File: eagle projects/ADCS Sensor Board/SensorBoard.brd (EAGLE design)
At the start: 91 x 91 mm, 134 parts, among them J5 HDR_10_EZFET_DEBUGGER, J6 MTI-1_8428-11B1-RK-TP, Q1 BC850SMD, Q2 IRF7507TRPBF, Q3 BSS138PS,115, Q4 BSS138PS,115, Q5 BSS138PS,115, Q6 BSS138PS,115, U1 MSP430F5529IPN, U2 LMV321, U3 ADS7841E_2K5, U4 LMV321, U5 LM20BIM7X_NOPB, U6 LMV321, U7 TLV9054IDR, U8 REF194GSZ-REEL7, U9 ADS7841E_2K5, Y1 32.768kHz, Y2 CSTCR4M00G15L99

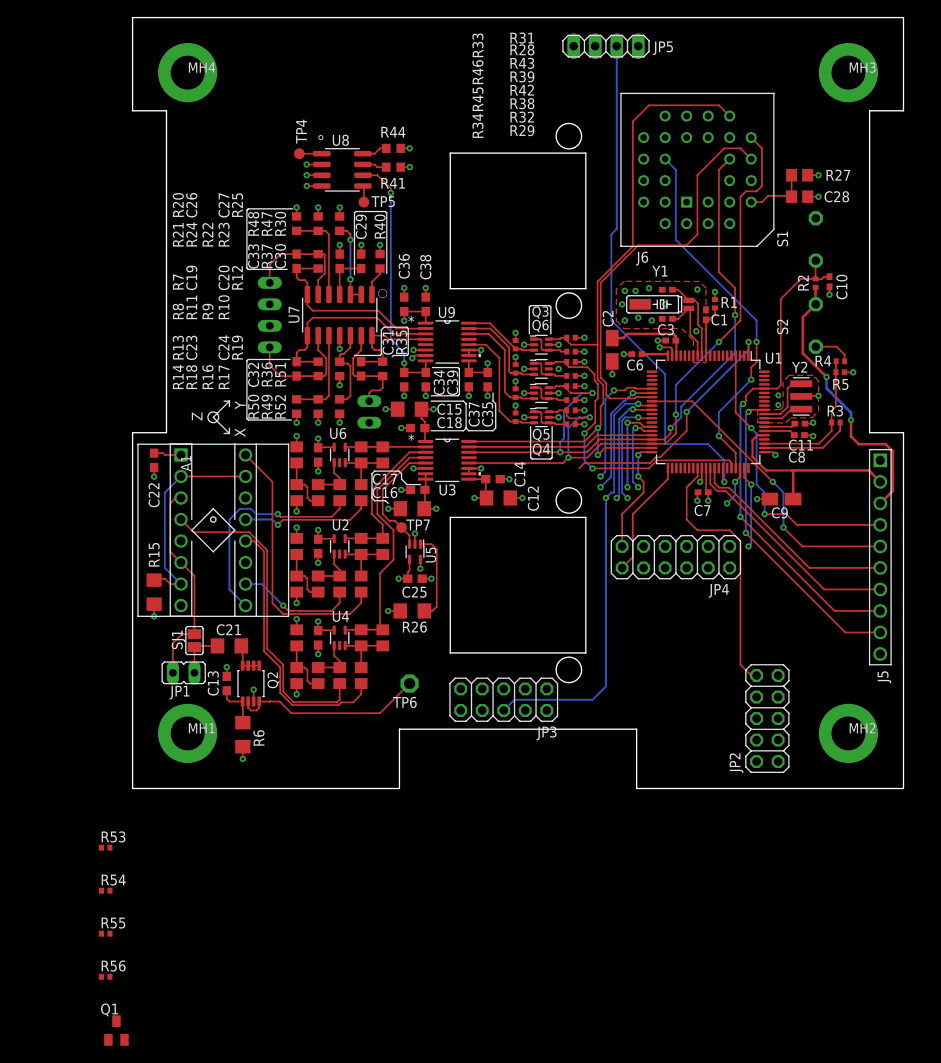
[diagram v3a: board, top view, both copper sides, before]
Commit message: Added files for Sunsensor Boards
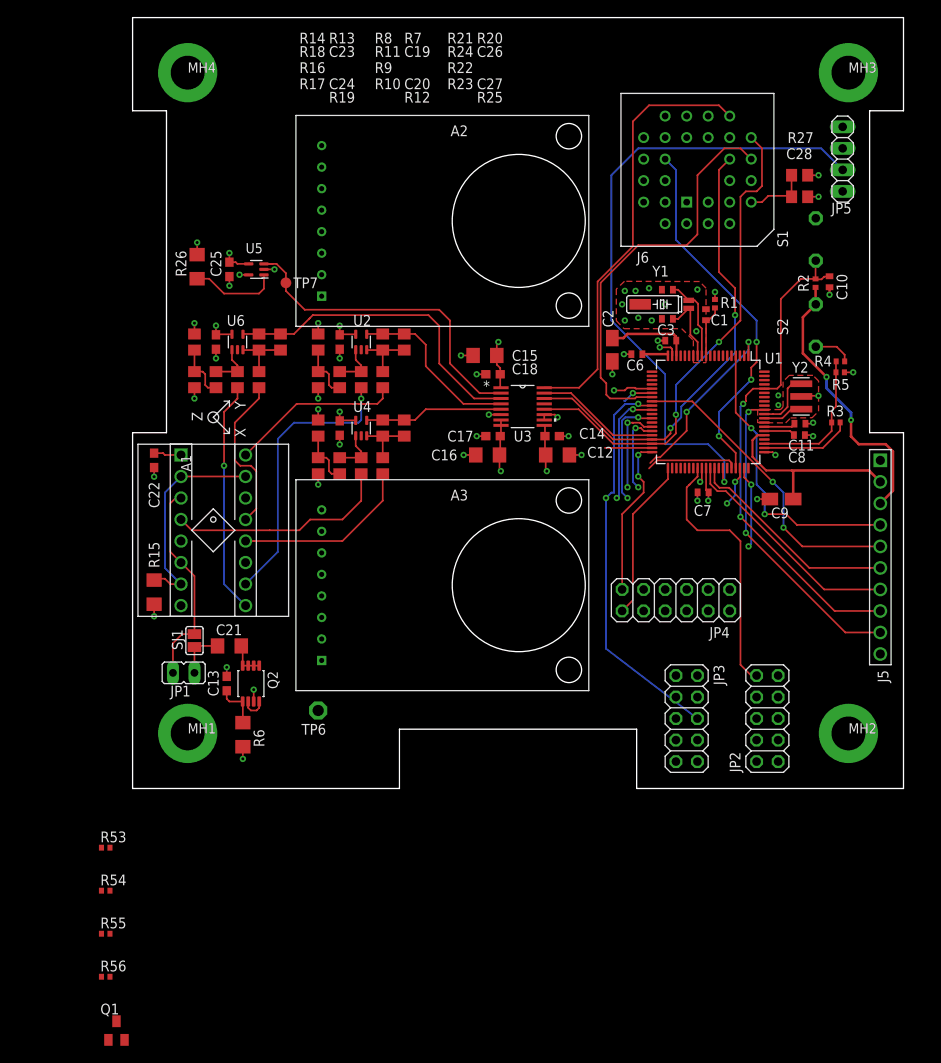
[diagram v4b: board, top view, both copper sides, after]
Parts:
- removed C29: 4.7u, rcl:C0603
- removed C30, C37, C38, C39: 0.1u, rcl:C0603
- removed C31, C32, C33: 9.1p, rcl:C0603
- removed C34, C35, C36: 1u, rcl:C0603
- removed D1, D2, D3: SFH2430, my_library:JP1Y_LED_SCREEN
- removed Q3, Q4, Q5, Q6: BSS138PS,115, my_library:SOT23-6P65_200X110L30X25N_BSS138PS,115
- removed R28, R29, R31, R32, R33, R34, R38, R39, R42, R43, R45, R46: 10k, rcl:R0402
- removed R30, R40, R41, R44: 5.1M, rcl:R0603
- removed R35, R36, R37: 698k, rcl:R0603
- removed R47, R48, R49, R50, R51, R52: 13.7k, rcl:R0603
- removed TP4, TP5: TPB1,27, testpad:B1,27
- removed U7: TLV9054IDR, my_library:SOIC14P127_865X600X175L83X41N_TLV9054IDR
- removed U8: REF194GSZ-REEL7, my_library:SOIC8P127_490X600X175L83X41N_REF194GSZ-REEL7
- removed U9: ADS7841E_2K5, my_library:DBQ16
- added A2, A3: ARDUCAM_OV5642, my_library:ARDUCAM
- C1, C10, C11, C3, C4, C5, C6, C7, C8: device rcl:0402 -> rcl:C0402
- moved R26 47.9 mm to (7.62, 61.6), turned to 270 degrees
- moved C25 42.6 mm to (11.4, 61.3), turned to 90 degrees
- moved U5 38.2 mm to (14.6, 61.3), turned to 90 degrees
- moved TP7 32.0 mm to (18.1, 59.7), turned to 90 degrees
- moved JP5 31.0 mm to (83.8, 74.3), turned to 270 degrees
- moved C23 24.9 mm to (24.4, 42.5)
- moved C24 24.9 mm to (29.5, 42.5)
- moved R13 24.9 mm to (21.9, 42.5)
- moved R14 24.9 mm to (21.9, 38.1)
- moved R16 24.9 mm to (27.0, 38.1)
- moved R17 24.9 mm to (29.5, 38.1)
- moved R18 24.9 mm to (24.4, 38.1)
- moved R19 24.9 mm to (32.1, 42.5)
- moved U4 24.9 mm to (27.0, 42.5)
- moved C19 24.3 mm to (24.4, 52.7)
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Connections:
- removed net +4V5: C34.1, C39.1, U8.6, U9.8
- removed net 0_DEGREES: C33.2, R37.2, U7.7, U9.2
- removed net 120_DEGREES: C32.2, R36.2, U7.8, U9.3
- removed net 240_DEGREES: C31.2, R35.2, U7.14, U9.4
- removed net 5V_!CS!_SUN_Z-: Q6.3, R46.1, U9.15
- removed net 5V_SPI_CLK: Q3.3, R33.1, U9.16
- removed net 5V_SPI_MISO: Q4.3, R34.1, U9.12
- removed net 5V_SPI_MOSI: Q5.3, R45.1, U9.14
- removed net IN2+BIAS: R47.1, R48.2, U7.5
- removed net IN3+BIAS: R49.1, R50.2, U7.10
- removed net IN4+BIAS: R51.1, R52.2, U7.12
- removed net N$14: Q3.1, Q3.4, R28.2
- removed net N$26: R30.2, U7.2, U7.3
- removed net N$27: R40.1, U7.1
- removed net N$28: C31.1, D3.1, R35.1, U7.13
- removed net N$30: Q5.1, Q5.4, R38.2
- removed net N$31: C32.1, D2.1, R36.1, U7.9
- removed net N$32: C33.1, D1.1, R37.1, U7.6
- removed net N$33: TP5.TP, U8.5
- removed net N$34: TP4.TP, U8.1
- removed net N$41: R41.2, U8.7
- removed net N$42: Q6.1, Q6.4, R39.2
- removed net N$43: R44.2, U8.8
- removed net N$48: Q4.1, Q4.4, R29.2
- new net !CS!_CAM_A: A2.1
- new net !CS!_CAM_B: A3.1
- new net N$17: A3.6
- new net PAYLOAD_MISO: A2.3, A3.3
- new net PAYLOAD_MOSI: A2.2, A3.2
- new net PAYLOAD_SCL: A2.8, A3.8
- new net PAYLOAD_SCLK: A2.4, A3.4
- new net PAYLOAD_SDA: A2.7, A3.7
- net !CS!_SUN_Z-: no longer Q6.6, R43.1
- net +3V3: no longer Q3.2, Q3.5, Q4.2, Q4.5, Q5.2, Q5.5, Q6.2, Q6.5, R28.1, R29.1, R31.2, R32.2, R38.1, R39.1, R42.2, R43.2
- net +5V: now also A2.6; no longer C29.1, C30.1, C35.1, C36.1, C37.1, C38.1, R33.2, R34.2, R45.2, R46.2, R47.2, R49.2, R51.2, U7.4, U8.2, U8.3, U9.1, U9.7, U9.9
- net BRD_TEMP_MEAS: now also U3.2; no longer U3.5
- net B_MEAS_X: now also U3.5; no longer U3.4
- net B_MEAS_Y: now also U3.4; no longer U3.3
- net B_MEAS_Z: now also U3.3; no longer U3.2
- net GND: now also A2.5, A3.5; no longer C29.2, C30.2, C34.2, C35.2, C36.2, C37.2, C38.2, C39.2, D1.2, D2.2, D3.2, R30.1, R40.2, R41.1, R44.1, R48.1, R50.1, R52.1, U7.11, U8.4, U9.10, U9.11, U9.6
- net UCB0_SPI_CLK: no longer Q3.6, R31.1
- net UCB0_SPI_MISO: no longer Q4.6, R32.1
- net UCB0_SPI_MOSI: no longer Q5.6, R42.1
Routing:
- net +4V5: track 30.2 -> 0.00 mm, vias 2 -> 0
- net B_MEAS_Z: track 9.46 -> 38.0 mm
- net HMC1053_RESET: track 52.5 -> 24.1 mm
- net +5V: track 50.7 -> 23.4 mm, vias 12 -> 0
- net UCB0_SPI_CLK: track 83.4 -> 56.5 mm, vias 2 -> 0
- net BRD_TEMP_MEAS: track 14.5 -> 40.0 mm
- net !CS!_SUN_Z-: track 36.1 -> 10.9 mm, vias 2 -> 0
- net 120_DEGREES: track 23.0 -> 0.00 mm
- net GND: track 70.3 -> 47.4 mm, vias 67 -> 48
- net UCB0_SPI_MOSI: track 77.0 -> 54.1 mm, vias 4 -> 2
- net 0_DEGREES: track 22.9 -> 0.00 mm
- net UCB0_SPI_MISO: track 78.7 -> 58.1 mm, vias 4 -> 2
- net OUT_A_N: track 14.1 -> 33.3 mm
- net +3V3: track 105.9 -> 90.0 mm, vias 32 -> 16
- net 5V_SPI_MISO: track 15.1 -> 0.00 mm
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- removed copper zone on layer 15, net +5V
- removed copper zone on layer 15, net +GND
- removed copper zone on layer 15, net GND
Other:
- outline, holes or cut-outs redrawn
- board text added: "Dalhousie Space Systems Lab"
- board text removed: "Q3"
- board text removed: "Q4"
- board text removed: "Q5"
- board text removed: "Q6"

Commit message: removed unused usb stuff from msp430
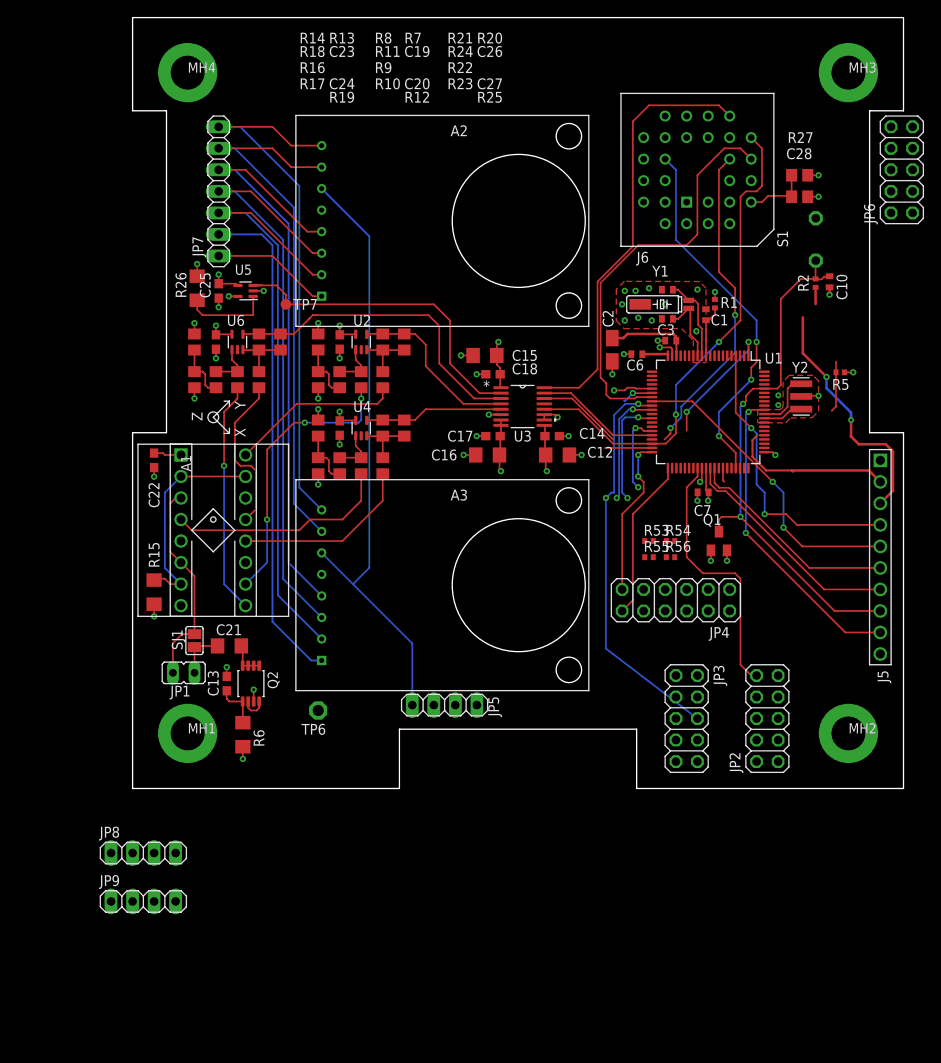
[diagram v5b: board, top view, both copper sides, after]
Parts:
- removed C11, C8: 220n, rcl:C0402
- removed C9: 4u7, rcl:A/3216-18R
- removed R3: 1k4, rcl:R0402
- removed R4: 100R, rcl:R0402
- removed S2: BSL, electricalmeter:PBTH
- added JP6: (no value), pinhead:2X05
- added JP7: (no value), pinhead:1X07
- added JP8, JP9: (no value), pinhead:1X04
- moved Q1 91.6 mm to (69.2, 29.2)
- moved R56 83.1 mm to (63.5, 27.3)
- moved JP5 79.8 mm to (36.8, 9.84), turned to 0 degrees
- moved R54 78.4 mm to (63.5, 29.2)
- moved R55 78.0 mm to (61.0, 27.3)
- moved R53 73.6 mm to (61.0, 29.2)
- moved C25 2.84 mm to (10.2, 58.7)
- moved U5 2.84 mm to (13.3, 58.7)
- moved R26 2.54 mm to (7.62, 59.1)
- moved TP7 2.54 mm to (18.1, 57.1)
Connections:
- removed net N$17: A3.6
- removed net P1.2: U1.23
- removed net P1.3: U1.24
- removed net P4.2: U1.47
- removed net P6.0: U1.77
- removed net P6.1: U1.78
- removed net P6.2: U1.79
- removed net P6.3: U1.80
- removed net P6.5: U1.2
- removed net P6.6: U1.3
- removed net P7.0: U1.5
- removed net P8.1: U1.16
- removed net P8.2: U1.17
- removed net TARGET_DP: R3.2, U1.62
- removed net TARGET_VUSB1: C8.1, U1.66
- removed net V1: C11.1, U1.67
- new net !COUNT_EN: JP6.2, U1.6
- new net !CS!_SPEED_X: JP6.1, U1.2
- new net !CS!_SPEED_Y: JP6.3, U1.3
- new net !CS!_SPEED_Z: JP6.5, U1.5
- new net !LOAD_SPEED: JP6.6, U1.8
- new net !SPEED_CLR: JP6.4, U1.7
- new net N$10: U1.59
- new net N$11: JP6.7
- new net N$13: JP6.9
- new net N$14: U1.64
- new net N$2: U1.33
- new net N$3: U1.58
- new net N$4: U1.53
- new net N$5: JP6.8
- new net N$6: JP6.10
- new net N$8: U1.34
- new net N$9: U1.55
- net !CS!_CAM_A: now also JP7.1
- net !CS!_CAM_B: now also JP7.2
- net !CS!_SUN_X-: now also U1.16; no longer U1.59
- net !CS!_SUN_Y-: now also U1.17; no longer U1.58
- net !CS!_SUN_Z+: now also JP9.2
- net !CS!_SUN_Z-: now also JP8.2, U1.15; no longer JP2.6, U1.56
- net +3V3: no longer S2.1
- net +5V: now also A3.6; no longer C9.+, U1.65
- net GND: now also U1.65; no longer C11.2, C8.2, C9.-
- net MAG_X_FIN: now also U1.23; no longer U1.33
- net MAG_X_RIN: now also U1.24; no longer U1.34
- net MSP430_ACTIVE: now also U1.47
- net MSP_OBC_RESET: now also Q1.B
- net N$1: now also U1.56; no longer Q1.B
- net N$12: now also U1.62; no longer R4.1, S2.2
- net PAYLOAD_MISO: now also JP7.4
- net PAYLOAD_MOSI: now also JP7.3
- net PAYLOAD_SCL: now also JP7.7
- net PAYLOAD_SCLK: now also JP7.5
- net PAYLOAD_SDA: now also JP7.6
- net RESERVED_1: now also U1.80
- net RESERVED_2: now also U1.79
- net RESERVED_3: now also U1.78
- net RESERVED_4: now also U1.77
- net TARGET_PUR: no longer R3.1, R4.2
- net UCB0_SPI_CLK: now also JP8.1, JP9.1
- net UCB0_SPI_MISO: now also JP8.4, JP9.4
- net UCB0_SPI_MOSI: now also JP8.3, JP9.3
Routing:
- net INIT_EPS_BURN_WIRE: track 76.1 -> 1.69 mm, vias 1 -> 0
- net PAYLOAD_MOSI: track 0.00 -> 72.4 mm
- net PAYLOAD_MISO: track 0.00 -> 72.3 mm
- net PAYLOAD_SCLK: track 0.00 -> 71.6 mm
- net +5V: track 23.4 -> 91.5 mm
- net PAYLOAD_SCL: track 0.00 -> 64.8 mm
- net PAYLOAD_SDA: track 0.00 -> 64.4 mm
- net !CS!_CAM_B: track 0.00 -> 59.0 mm
- net !CS!_CAM_A: track 0.00 -> 14.1 mm
- net TARGET_PUR: track 17.0 -> 6.03 mm
- net !CS!_SUN_Z-: track 10.9 -> 0.00 mm
- net TARGET_DP: track 10.8 -> 0.00 mm
- net MAG_X_RIN: track 10.7 -> 0.00 mm, vias 2 -> 0
- net !CS!_SUN_X-: track 9.72 -> 0.00 mm, vias 2 -> 0
- net UCB0_SPI_MOSI: track 54.1 -> 48.0 mm
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
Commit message: Finished up pinout connectors on sensor board
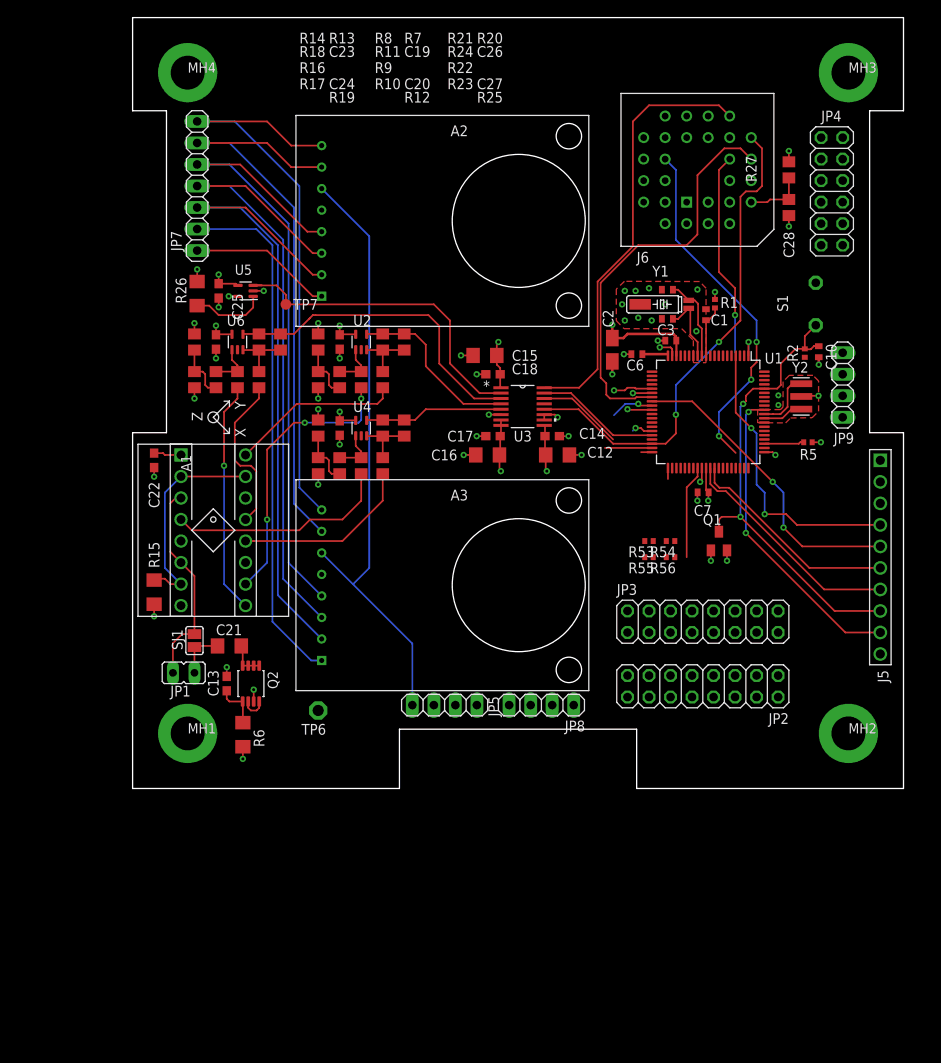
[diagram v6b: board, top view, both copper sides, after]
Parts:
- removed JP6: (no value), pinhead:2X05
- JP2, JP3: device pinhead:2X05 -> pinhead:2X08
- moved JP9 102.6 mm to (83.8, 47.6), turned to 90 degrees
- moved JP4 51.7 mm to (82.5, 70.5), turned to 270 degrees
- moved JP8 50.1 mm to (48.3, 9.84), turned to 180 degrees
- moved JP3 11.6 mm to (67.3, 19.7), turned to 0 degrees
- moved R5 9.09 mm to (79.7, 40.9)
- moved JP2 8.52 mm to (67.3, 12.1), turned to 180 degrees
- moved C10 8.35 mm to (81.0, 51.6)
- moved R2 8.35 mm to (79.3, 51.4)
- moved S1 7.62 mm to (80.6, 59.7)
- moved JP7 2.62 mm to (7.62, 71.1)
- moved C28 1.80 mm to (77.5, 68.6), turned to 90 degrees
- moved R27 1.42 mm to (77.5, 73.0), turned to 270 degrees
- moved R26 0.63 mm to (7.62, 58.4)
- turned R53 to 180 degrees
- turned R54 to 180 degrees
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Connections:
- removed net N$1: U1.56
- removed net N$10: U1.59
- removed net N$11: JP6.7
- removed net N$12: U1.62
- removed net N$13: JP6.9
- removed net N$14: U1.64
- removed net N$2: U1.33
- removed net N$3: U1.58
- removed net N$4: U1.53
- removed net N$5: JP6.8
- removed net N$6: JP6.10
- removed net N$8: U1.34
- removed net N$9: U1.55
- removed net P1.0: U1.21
- removed net P1.1: U1.22
- removed net P3.5: U1.42
- removed net P3.6: U1.43
- removed net P3.7: U1.44
- removed net P4.0: U1.45
- removed net P4.1: U1.46
- new net !CS!_CURRENT_SENSE_1: JP2.11, U1.9
- new net !CS!_CURRENT_SENSE_2: JP2.13, U1.10
- new net RW_X_DIR: JP3.7, U1.75
- new net RW_X_OUTFG: JP3.13, U1.57
- new net RW_X_SPEED_CTRL: JP3.1, U1.32
- new net RW_Y_DIR: JP3.9, U1.74
- new net RW_Y_OUTFG: JP3.15, U1.56
- new net RW_Y_SPEED_CTRL: JP3.3, U1.33
- new net RW_Z_DIR: JP3.11, U1.73
- new net RW_Z_OUTFG: JP3.16, U1.55
- new net RW_Z_SPEED_CTRL: JP3.5, U1.34
- net !COUNT_EN: now also JP2.5; no longer JP6.2
- net !CS!_SPEED_X: now also JP2.8; no longer JP6.1
- net !CS!_SPEED_Y: now also JP2.10; no longer JP6.3
- net !CS!_SPEED_Z: now also JP2.12; no longer JP6.5
- net !CS!_SUN_X+: now also JP2.16; no longer JP2.10
- net !CS!_SUN_X-: now also JP2.14, U1.15; no longer JP2.8, U1.16
- net !CS!_SUN_Y+: now also JP2.3, U1.47; no longer JP2.4, U1.35
- net !CS!_SUN_Y-: now also JP2.1, U1.16; no longer JP2.2, U1.17
- net !CS!_SUN_Z+: now also U1.46; no longer U1.32
- net !CS!_SUN_Z-: now also U1.17; no longer U1.15
- net !LOAD_SPEED: now also JP2.9; no longer JP6.6
- net !SPEED_CLR: now also JP2.7; no longer JP6.4
- net +3V3: now also JP4.1; no longer JP4.3
- net +5V: no longer J5.2
- net ACT_BRD_3V_PRESENT: now also JP2.15; no longer JP3.7
- net ACT_BRD_5V_PRESENT: now also JP3.14; no longer JP3.5
- net MAG_X_FIN: now also JP3.10
- net MAG_X_RIN: now also JP3.12
- net MAG_Z_FIN: no longer JP3.10
- net MAG_Z_RIN: no longer JP3.9
- net MSP430_ACTIVE: now also U1.35; no longer U1.47
- net MTI_DRDY: now also U1.53; no longer U1.57
- net SEN_BRD_5V_PRESENT: now also JP4.3; no longer JP4.1
- net UCB0_SPI_CLK: now also JP2.2; no longer JP2.1
- net UCB0_SPI_MISO: now also JP2.4; no longer JP2.3
- net UCB0_SPI_MOSI: now also JP2.6; no longer JP2.5
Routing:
- net MAG_Y_FIN: track 46.9 -> 5.12 mm, vias 2 -> 1
- net +3V3: track 87.8 -> 58.6 mm, vias 16 -> 15
- net !CS!_SUN_X+: track 31.0 -> 11.0 mm
- net +5V: track 91.5 -> 72.2 mm
- net UCA0RXD: track 19.5 -> 1.67 mm
- net UCA0TXD: track 19.0 -> 1.31 mm, vias 2 -> 0
- net UCB0_SPI_MOSI: track 48.0 -> 34.3 mm, vias 2 -> 1
- net !CS!_SUN_Z+: track 13.1 -> 0.00 mm, vias 2 -> 0
- net HMC1053_RESET: track 18.2 -> 5.63 mm, vias 2 -> 1
- net MAG_Y_RIN: track 13.8 -> 2.92 mm, vias 2 -> 1
- net !CS!_SUN_Y+: track 9.46 -> 0.00 mm, vias 2 -> 0
- net RST/SBWTDIO: track 63.8 -> 55.8 mm
- net PAYLOAD_SDA: track 64.4 -> 70.1 mm
- net PAYLOAD_MOSI: track 72.4 -> 78.0 mm
- net PAYLOAD_SCLK: track 71.6 -> 77.2 mm
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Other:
- board text removed: "BSL"
